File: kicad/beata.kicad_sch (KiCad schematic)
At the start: 5 parts, among them J1 Sound Sensor, J2 PIR Motion Sensor, J3 Adafruit BME680, U1 Pico, U2 Pico

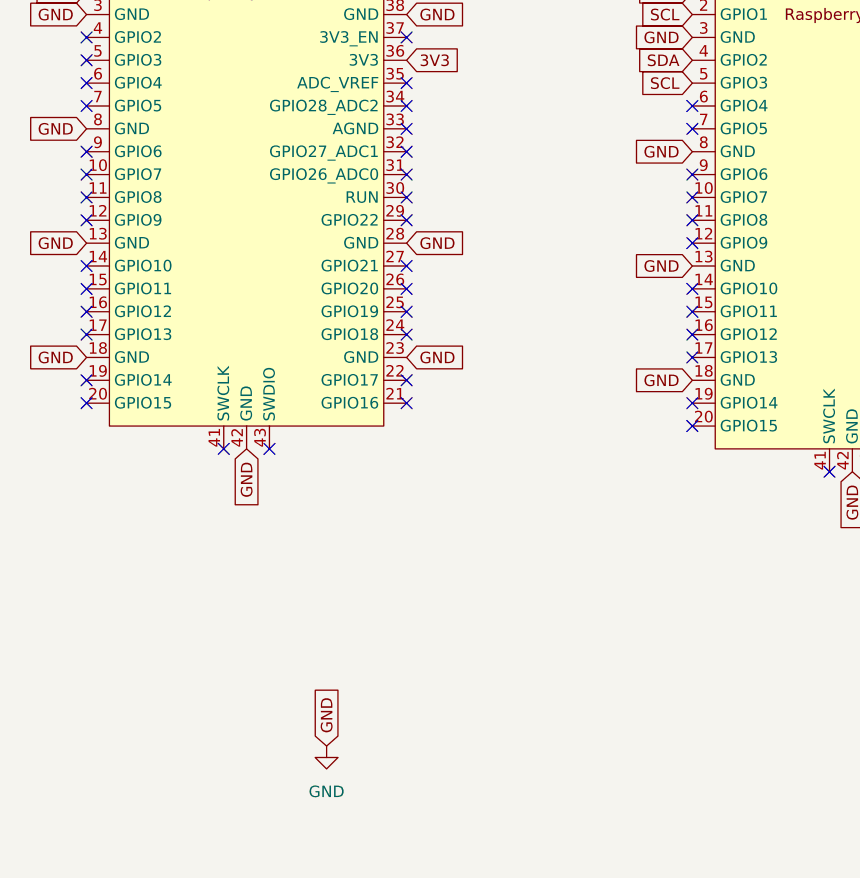
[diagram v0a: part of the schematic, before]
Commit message: added led
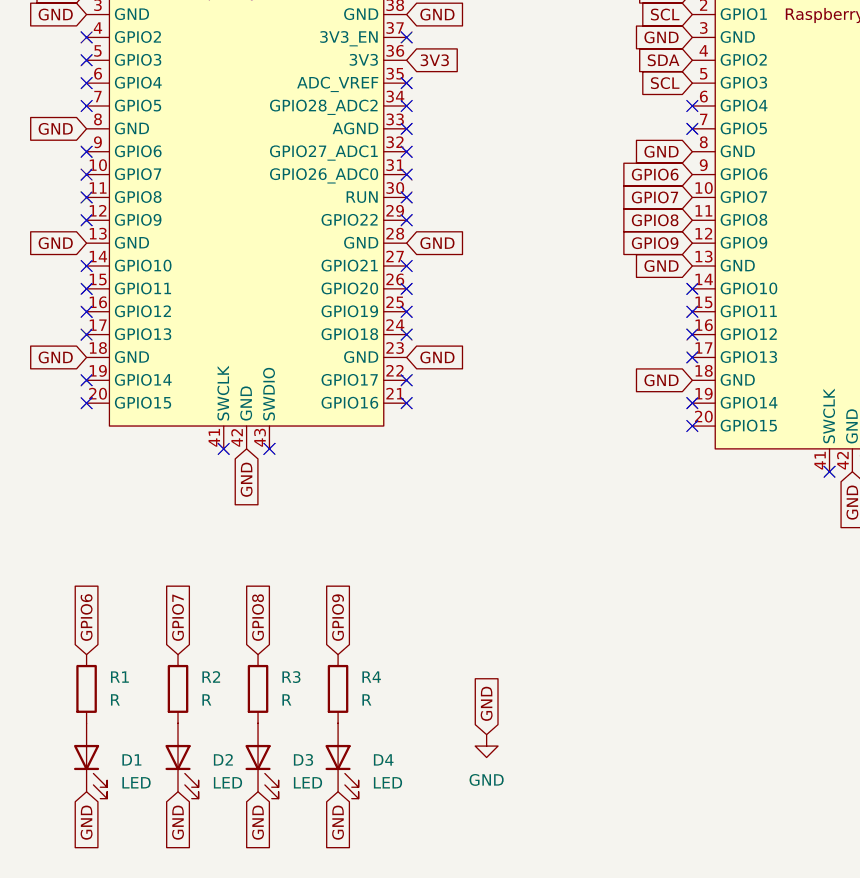
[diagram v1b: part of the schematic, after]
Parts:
- added D1, D2, D3, D4: LED, symbol Device:LED
- added R1, R2, R3, R4: R, symbol Device:R
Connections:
- net GND: now also D1.1 (K), D2.1 (K), D3.1 (K), D4.1 (K)
- net GPIO7: now reaches U2.10 (GPIO7)
- net GPIO7: now also R2.1
- net GPIO8: now reaches U2.11 (GPIO8)
- net GPIO8: now also R3.1
- net GPIO9: now reaches U2.12 (GPIO9)
- net GPIO9: now also R4.1
- net GPIO6: now reaches U2.9 (GPIO6)
- net GPIO6: now also R1.1
- new net: D1.2 (A), R1.2
- new net: D2.2 (A), R2.2
- new net: D4.2 (A), R4.2
- new net: D3.2 (A), R3.2
- no-connect marks 60 -> 56

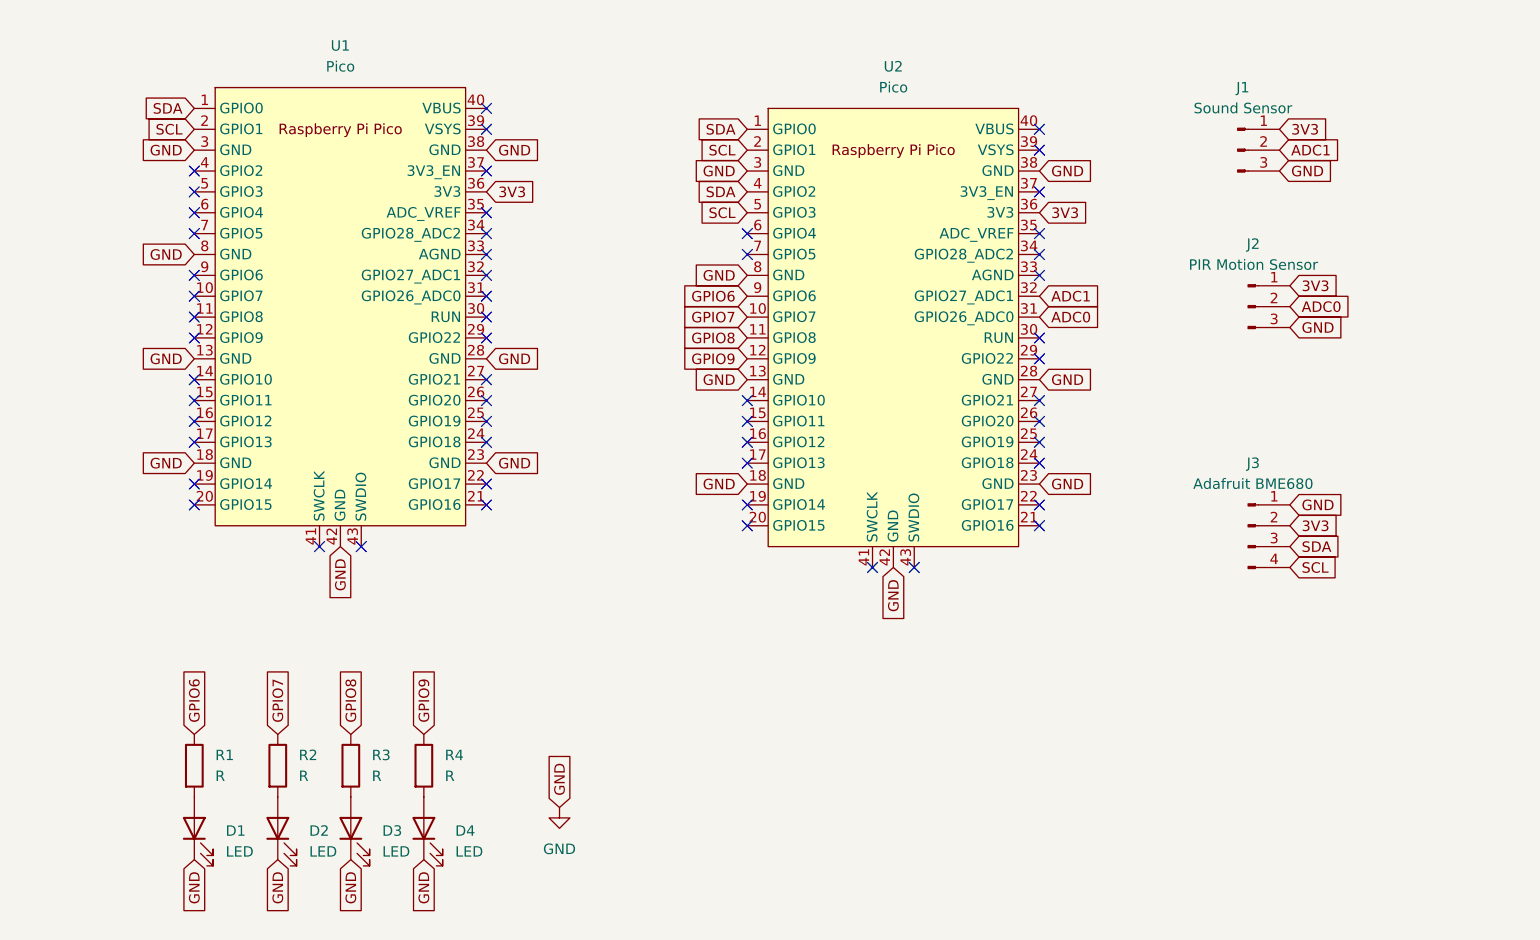
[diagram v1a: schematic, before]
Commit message: added more leds and updated i2c
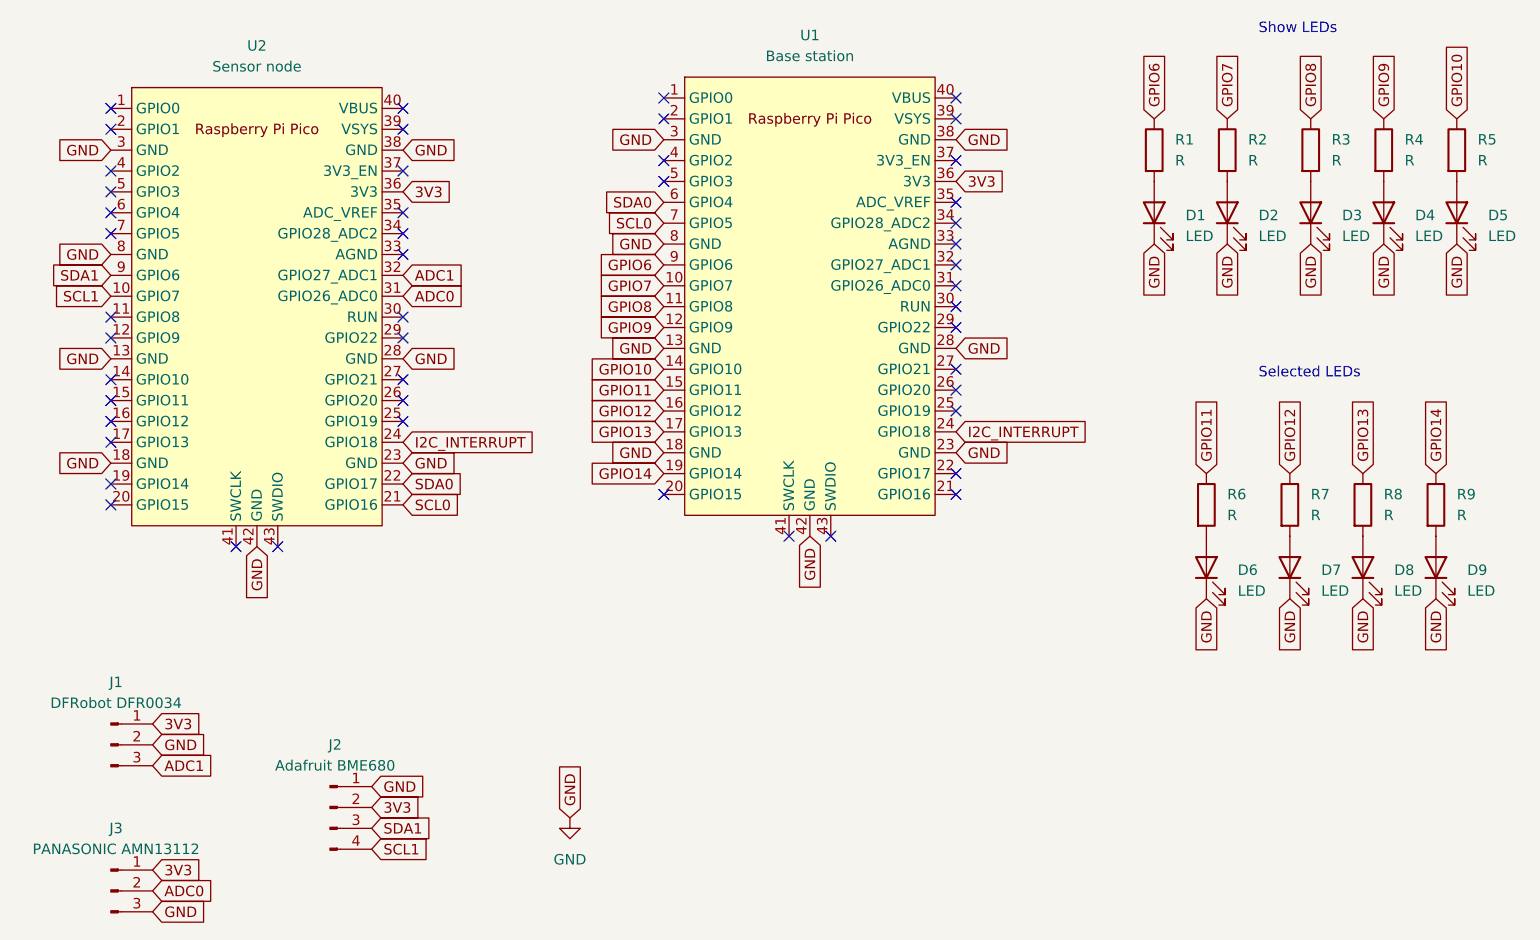
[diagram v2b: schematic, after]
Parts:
- added D1, D2, D3, D4, D5: LED, symbol Device:LED
- added R1, R2, R3, R4, R5: R, symbol Device:R
- J1: value Sound Sensor -> DFRobot DFR0034
- J3: renamed from J2; value PIR Motion Sensor -> PANASONIC AMN13112
- U1: value Pico -> Base station
- U2: value Pico -> Sensor node
- renumbered D1 to D6, D2 to D7, D3 to D8, D4 to D9, J3 to J2, R1 to R6, R2 to R7, R3 to R8, R4 to R9
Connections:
- net ADC1: now also J1.3 (Pin_3); no longer J1.2 (Pin_2)
- net GND: now also J1.2 (Pin_2), D1.1 (K), D2.1 (K), D3.1 (K), D4.1 (K), D5.1 (K); no longer J1.3 (Pin_3)
- net GPIO6: now also U1.9 (GPIO6), R1.1; no longer R6.1, U2.9 (GPIO6)
- net GPIO7: now also U1.10 (GPIO7), R2.1; no longer R7.1, U2.10 (GPIO7)
- net GPIO8: now also U1.11 (GPIO8), R3.1; no longer R8.1, U2.11 (GPIO8)
- net GPIO9: now also U1.12 (GPIO9), R4.1; no longer R9.1, U2.12 (GPIO9)
- net SCL0: now reaches U2.21 (GPIO16)
- net SCL0: now also U1.7 (GPIO5)
- net SDA0: now reaches U2.22 (GPIO17)
- net SDA0: now also U1.6 (GPIO4)
- net I2C_INTERRUPT: now reaches U2.24 (GPIO18)
- net I2C_INTERRUPT: now also U1.24 (GPIO18)
- net GPIO10: now reaches U1.14 (GPIO10)
- net GPIO10: now also R5.1
- net GPIO11: now reaches U1.15 (GPIO11)
- net GPIO11: now also R6.1
- net GPIO12: now reaches U1.16 (GPIO12)
- net GPIO12: now also R7.1
- net GPIO13: now reaches U1.17 (GPIO13)
- net GPIO13: now also R8.1
- net GPIO14: now reaches U1.19 (GPIO14)
- net GPIO14: now also R9.1
- removed net SCL: J2.4 (Pin_4), U1.2 (GPIO1), U2.2 (GPIO1), U2.5 (GPIO3)
- removed net SDA: J2.3 (Pin_3), U1.1 (GPIO0), U2.1 (GPIO0), U2.4 (GPIO2)
- new net: D2.2 (A), R2.2
- new net: D3.2 (A), R3.2
- new net: D4.2 (A), R4.2
- new net: D1.2 (A), R1.2
- new net: D5.2 (A), R5.2
- new net SCL1: J2.4 (Pin_4), U2.10 (GPIO7)
- new net SDA1: J2.3 (Pin_3), U2.9 (GPIO6)
- no-connect marks 56 -> 49
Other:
- note added: "Selected LEDs"
- note added: "Show LEDs"
- moved on the sheet: D6, D7, D8, D9, J1, J2, J3, R6, R7, R8, R9, U1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
